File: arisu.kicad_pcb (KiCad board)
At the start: 2 copper layers, 339.1 x 118.7 mm, 176 parts, among them J1 USB_B_Micro, SW1 SW_Push, SW10 SW_Push, SW11 SW_Push, SW12 SW_Push, SW13 SW_Push, SW14 SW_Push, SW15 SW_Push, SW16 SW_Push, SW17 SW_Push, SW18 SW_Push, SW19 SW_Push, SW2 SW_Push, SW20 SW_Push, SW21 SW_Push, SW22 SW_Push, SW23 SW_Push, SW24 SW_Push, SW25 SW_Push, SW26 SW_Push, SW27 SW_Push, SW28 SW_Push, SW29 SW_Push, SW3 SW_Push, SW30 SW_Push, SW31 SW_Push, SW32 SW_Push, SW33 SW_Push, SW34 SW_Push, SW35 SW_Push, SW36 SW_Push, SW37 SW_Push, SW38 SW_Push, SW39 SW_Push, SW4 SW_Push, SW40 SW_Push, SW41 SW_Push, SW42 SW_Push, SW43 SW_Push, SW44 SW_Push, SW45 SW_Push, SW46 SW_Push, SW47 SW_Push, SW48 SW_Push, SW49 SW_Push, SW5 SW_Push, SW50 SW_Push, SW51 SW_Push, SW52 SW_Push, SW53 SW_Push, SW54 SW_Push, SW55 SW_Push, SW56 SW_Push, SW57 SW_Push, SW58 SW_Push, SW59 SW_Push, SW6 SW_Push, SW60 SW_Push, SW61 SW_Push, SW62 SW_Push, SW63 SW_Push, SW64 SW_Push, SW65 SW_Push, SW66 SW_Push, SW67 SW_Push, SW7 SW_Push, SW8 SW_Push, SW9 SW_Push, U1 USBLC6-2SC6, U2 ATmega32U4-AU, Y1 Crystal_GND24

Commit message: Initial project update
- Imported FateParts library
- Updated schematic with full backspace switch and stepped capslock switch
- Added new switch footprints to layout
- Updated some traces in layout
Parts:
- removed G*** (x2): LOGO, arisu:arisu-logo
- added SW3CL1: SW_Push, FateParts-MXSwitch:SW_Cherry_MX_1.25u_PCB, F.Cu at (29.6, 67.3)
- added SW59B1: SW_Push, FateParts-MXSwitch:SW_Cherry_MX_2.00u_PCB, F.Cu at (294.1, 29.2)
- moved D3 4.73 mm to (38.3, 80.6)
- renumbered PF6 to J10, PF7 to J11, VCC to J12, D+ to J13, D- to J14, GND to J15, MISO to J2, VCC to J3, SCK to J4, MOSI to J5, RES to J6, GND to J7, PF4 to J8, PF5 to J9
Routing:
- net Net-(D59-Pad2): track 4.91 -> 14.4 mm
- net /col13: track 269.0 -> 274.6 mm
- net Net-(D3-Pad2): track 4.91 -> 9.68 mm
- net /col0: track 204.4 -> 209.2 mm
- net /row2: track 399.4 -> 404.0 mm
- net /MISO: track 272.2 -> 273.9 mm

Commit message: Changed mini-USB to USB-C
- Removed mini-USB from schematic and layout
- Added USB-C to schematic and layout
- Added 5k1 resistors for CC1 and CC2 pins, added to layout
- Added bump-out on PCB for USB-C connector to protrude slightly
- Rerouted traces as necessary
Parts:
- added R5: 5k1, Resistor_SMD:R_0805_2012Metric_Pad1.15x1.40mm_HandSolder, B.Cu at (152.3, 31.4)
- added R6: 5k1, Resistor_SMD:R_0805_2012Metric_Pad1.15x1.40mm_HandSolder, B.Cu at (159.3, 35.8)
- J1: value USB_B_Micro -> HRO_TYPE-C-31-M-12; footprint Connectors_USB:USB_Micro-B_Molex-105017-0001 -> FateParts-USBC:USB_C_Receptacle_HRO_TYPE-C-31-M-12
- moved J1 5.73 mm to (175.5, 20.6)
- moved D59 5.09 mm to (295.4, 42.5)
- moved C3 1.16 mm to (184.3, 30.2)
- moved C4 1.16 mm to (182.3, 30.2)
- moved D63 0.28 mm to (319.7, 42.7)
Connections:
- J13 pad 1: Net-(J1-Pad3) -> Net-(J1-PadA6)
- J14 pad 1: Net-(J1-Pad2) -> Net-(J1-PadA7)
- R1 pad 2: Net-(J1-Pad3) -> Net-(J1-PadA6)
- R2 pad 2: Net-(J1-Pad2) -> Net-(J1-PadA7)
- U1 pad 4: Net-(J1-Pad2) -> Net-(J1-PadA7)
- U1 pad 6: Net-(J1-Pad3) -> Net-(J1-PadA6)
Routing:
- net Net-(J1-Pad3): track 47.8 -> 0.00 mm
- net Net-(J1-Pad2): track 45.1 -> 0.00 mm
- net Net-(J1-PadA6): track 0.00 -> 39.5 mm
- net Net-(J1-PadA7): track 0.00 -> 33.0 mm
- net Net-(J1-PadA5): track 0.00 -> 24.4 mm, vias 0 -> 2
- net Net-(J1-PadB5): track 0.00 -> 23.6 mm, vias 0 -> 2
- net GND: track 71.6 -> 62.9 mm, vias 12 -> 14
- net VCC: track 205.4 -> 211.5 mm, vias 9 -> 11
- net Net-(D59-Pad2): track 14.4 -> 17.8 mm
- net Net-(C4-Pad1): track 8.19 -> 8.85 mm
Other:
- board size 339.1 x 118.7 mm -> 339.1 x 121 mm
- board text added: "Fate Design - Arisu Rev 1.1 Mods by CorruptedJef and robotictomato"
- board text removed: "Fate Design Rev 1.1"

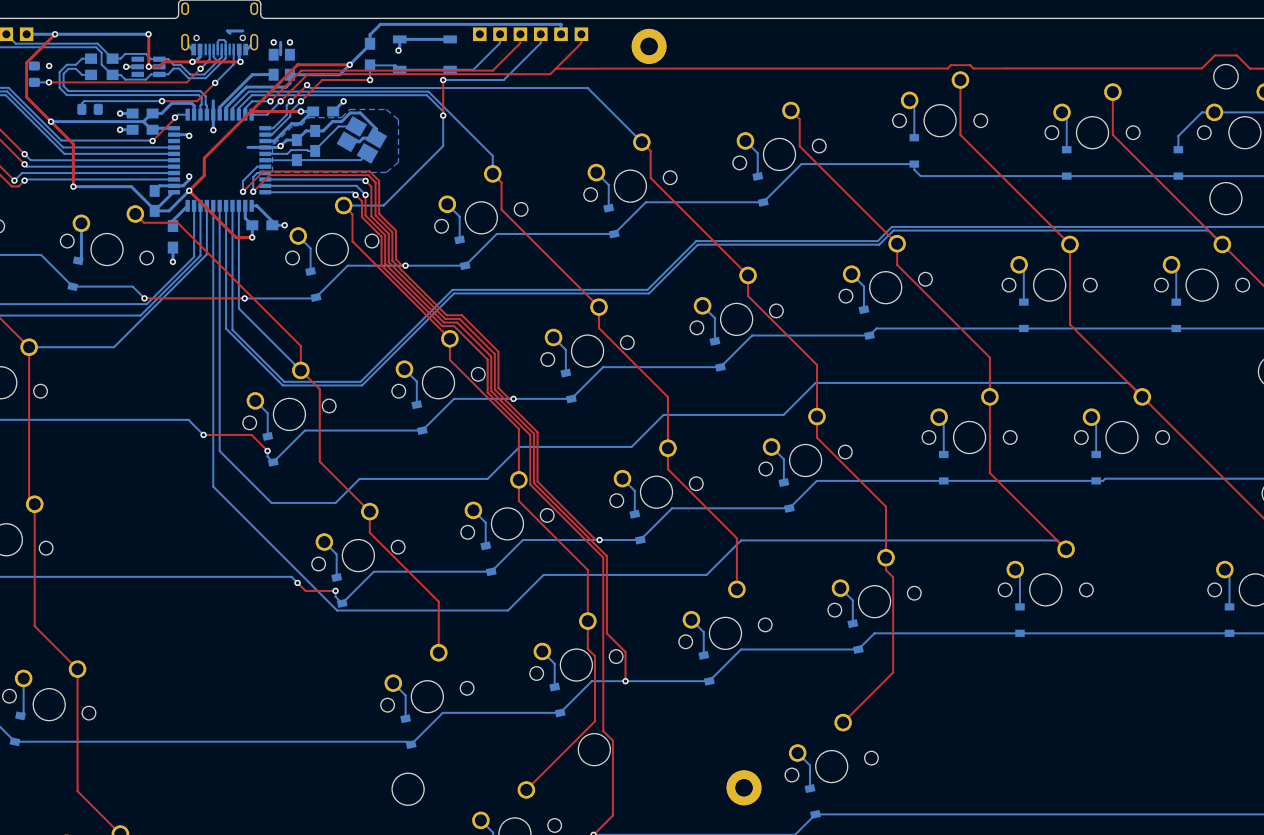
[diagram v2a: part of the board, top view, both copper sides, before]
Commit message: Additional trace cleanup
Some more trace cleanup for the USB data lines from the connector.
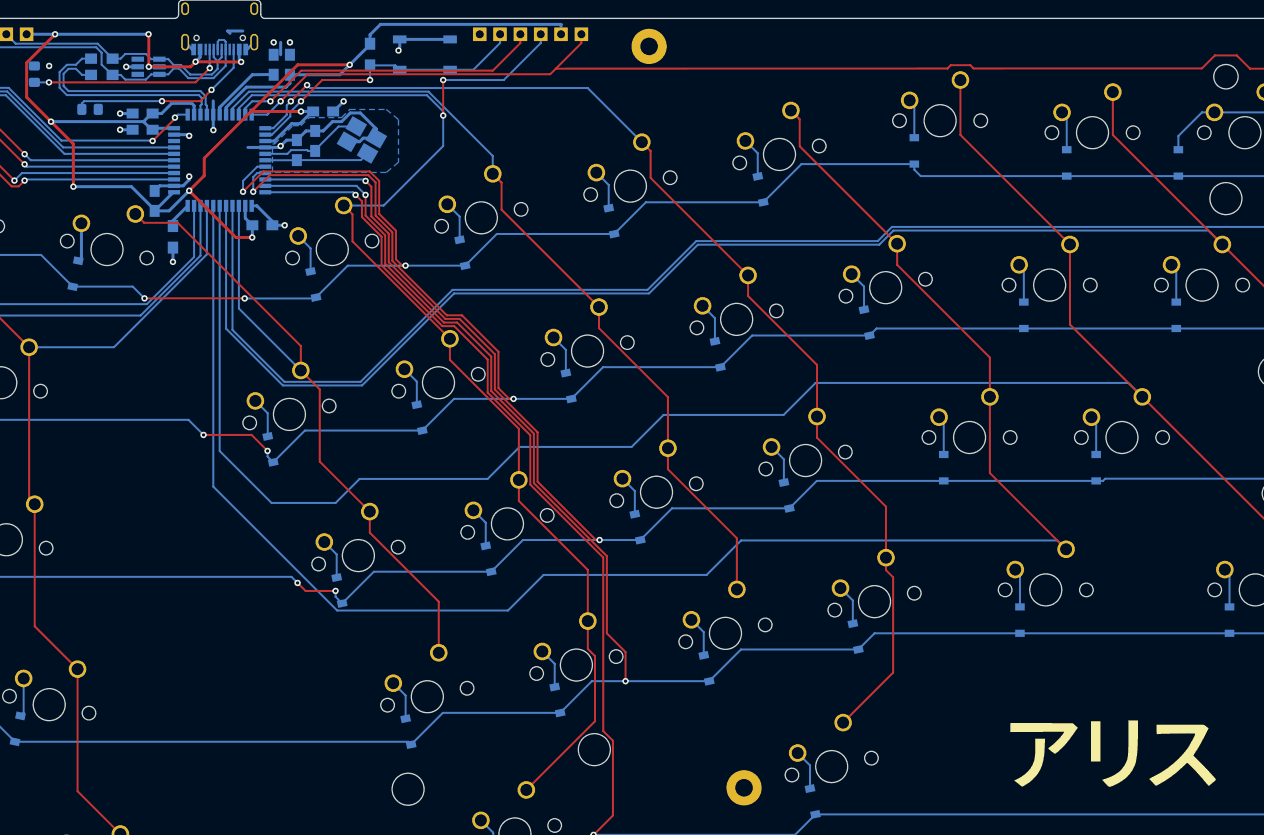
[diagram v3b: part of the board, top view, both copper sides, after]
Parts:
- added G***: LOGO, arisu:arisu-logo, B.Cu at (285.9, 112.9)
- added G***: LOGO, arisu:arisu-logo, F.Cu at (287.2, 116.3)
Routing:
- net Net-(J1-PadA5): track 24.4 -> 25.0 mm
- net Net-(J1-PadA7): track 33.0 -> 33.6 mm
- net Net-(J1-PadA6): track 39.5 -> 40.1 mm

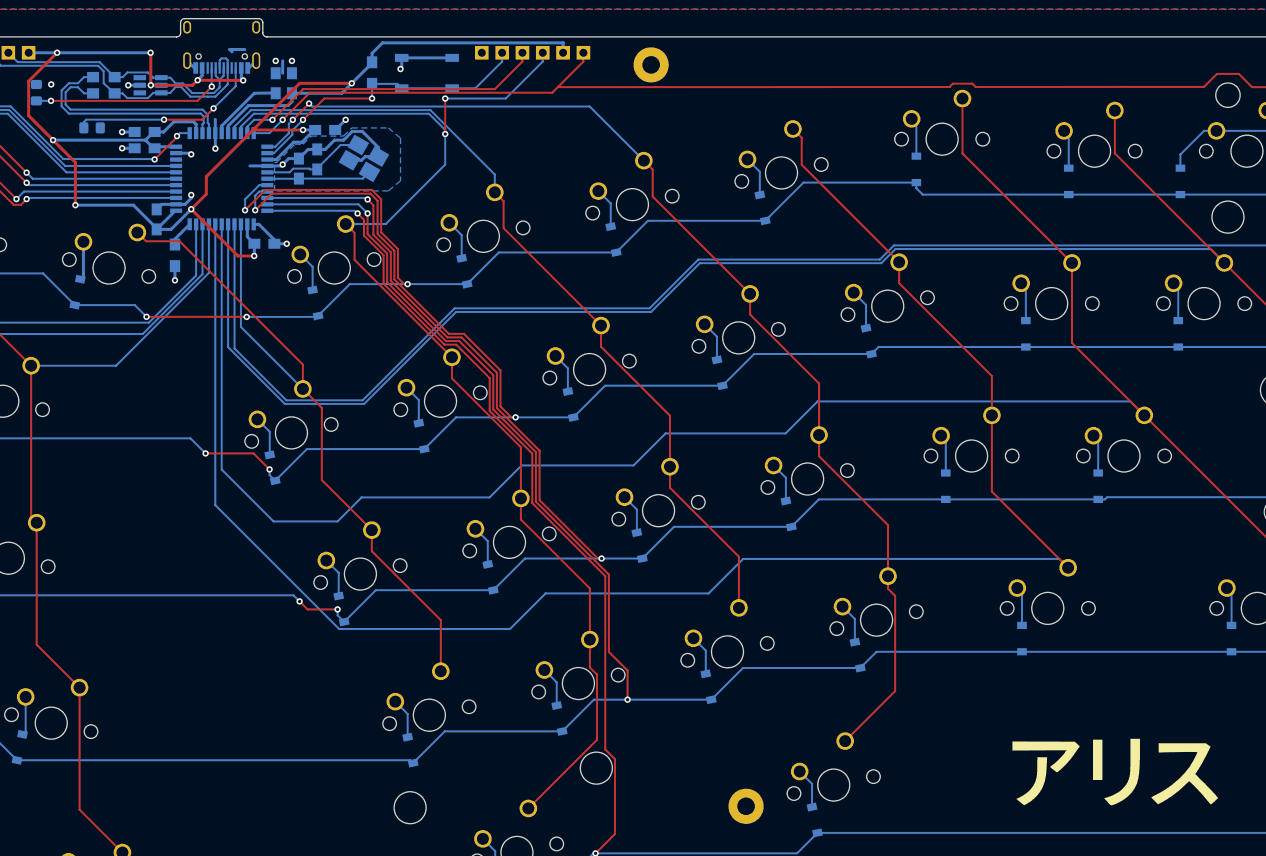
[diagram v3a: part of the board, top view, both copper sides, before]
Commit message: Addition of BOM and position files
- Added JLCPCB part numbers in BOM and exported
- Exported component positioning file
- Some minor cleanup of traces and silkscreen legend positions.
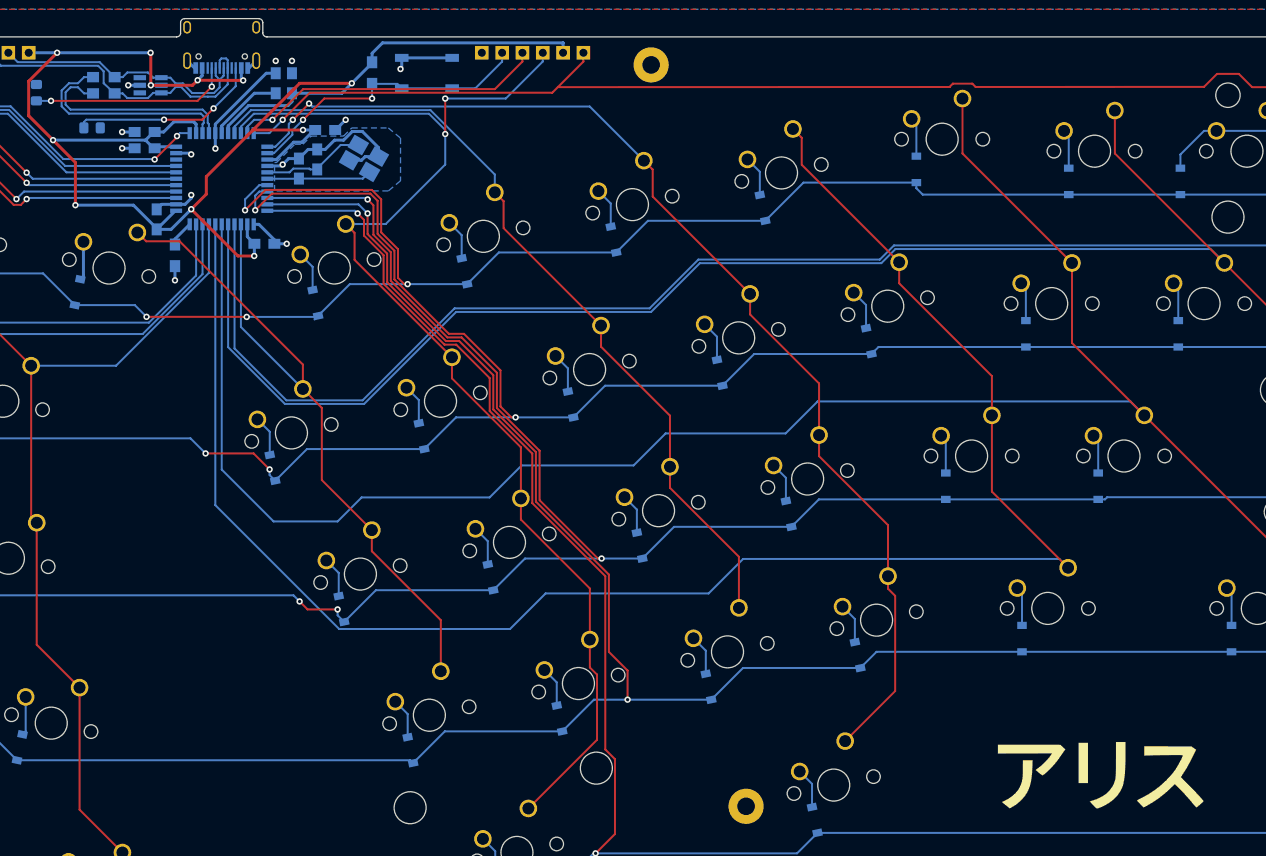
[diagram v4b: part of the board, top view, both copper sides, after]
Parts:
- removed the G*** at (285.9, 112.9)
- removed the G*** at (287.2, 116.3)
- added G***: LOGO, arisu:arisu-logo, B.Cu at (285.5, 113.4)
- added G***: LOGO, arisu:arisu-logo, F.Cu at (285.4, 116.7)
- USB1: renamed from J1; value HRO_TYPE-C-31-M-12 -> USB_C_Receptacle_HRO_TYPE-C-31-M-12; footprint FateParts-USBC:USB_C_Receptacle_HRO_TYPE-C-31-M-12 -> USB_Type-C:USB_C_Receptacle_HRO_TYPE-C-31-M-12
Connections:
- D66 pad 1: /row3 -> Net-(D66-Pad1)
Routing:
- net GND: track 62.9 -> 66.5 mm, vias 14 -> 13
- net Net-(C4-Pad1): track 8.85 -> 9.35 mm
